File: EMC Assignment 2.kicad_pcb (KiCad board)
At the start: 4 copper layers, 120 x 53 mm, 91 parts, among them IC1 LP2985AIM5-3.0_NOPB, J1 M40-3200445R, U1 LT8636, U2 ATMEGA16U2-MU, U3 ATMEGA328P-PU, U8 OPA4350EA_250, X2 USB, Y1 16MHz, Y2 16M

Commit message: Good state
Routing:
- net /PB4: track 35.9 -> 28.1 mm

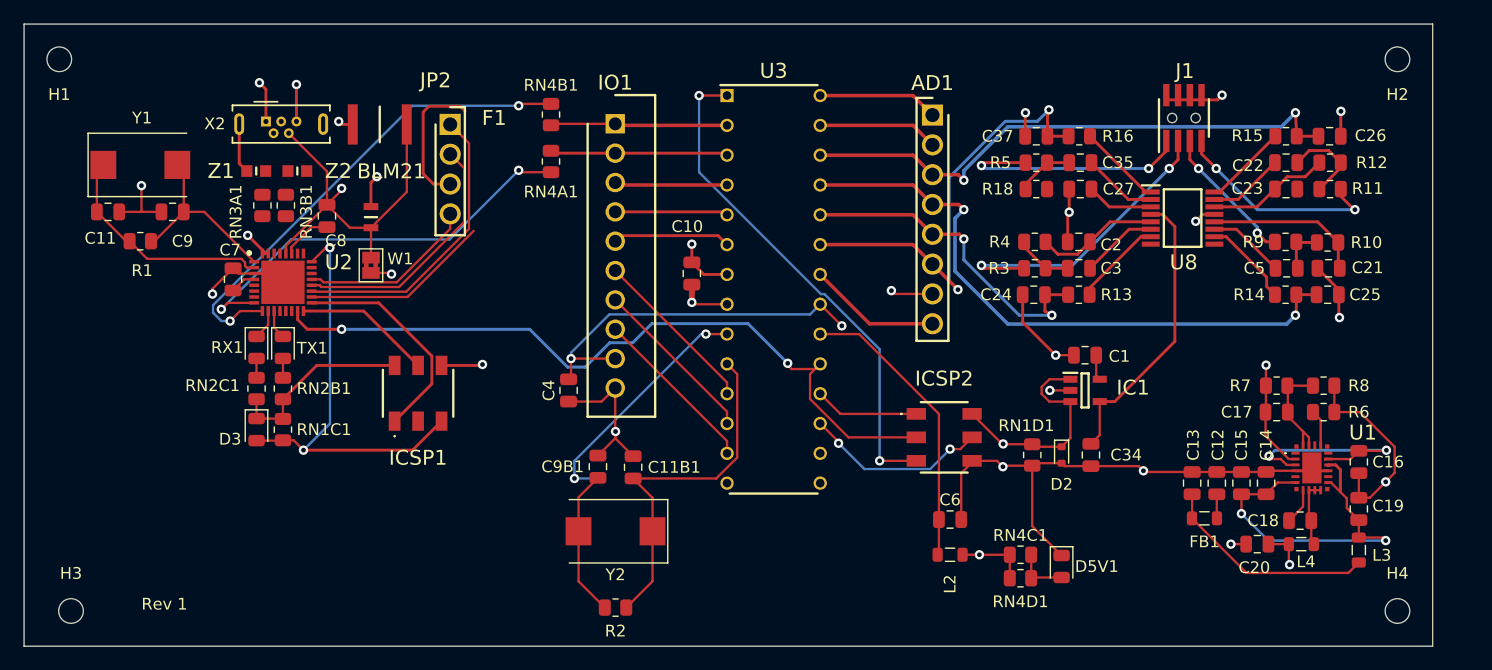
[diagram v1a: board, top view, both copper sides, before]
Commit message: Fixed majority of DRC issues. Only differential pair needs to be fixed up
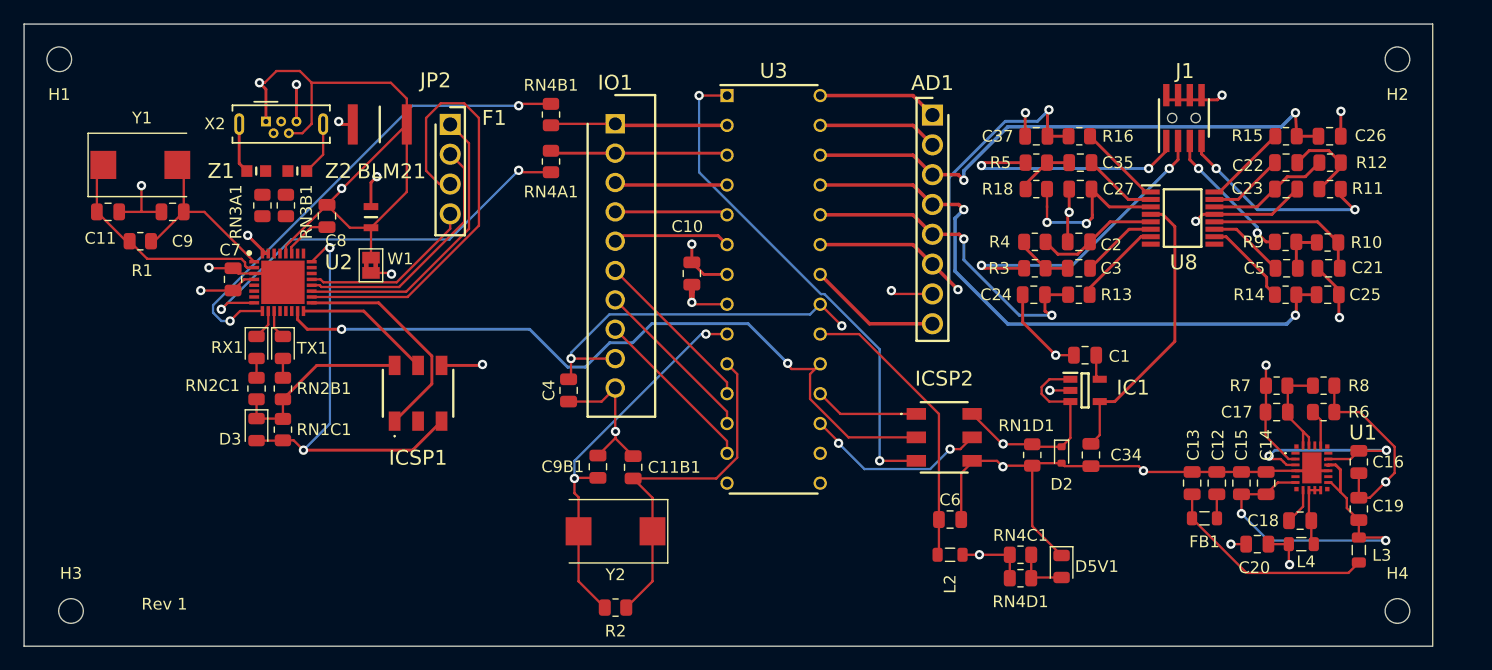
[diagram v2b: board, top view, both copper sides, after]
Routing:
- net /UGND: track 35.7 -> 57.9 mm
- net /PB4: track 28.1 -> 38.5 mm
- net Net-(U8-+IN_A): track 5.68 -> 15.4 mm, vias 0 -> 2
- net GND: track 139.9 -> 147.0 mm
- net Net-(X2-Shield): track 4.27 -> 8.85 mm
- net +5V: track 49.3 -> 52.0 mm, vias 7 -> 8
- net Net-(U3-PB6_(PCINT6/XTAL1/TOSC1)): track 33.6 -> 33.1 mm

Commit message: Fixed differential lines with new USB footprint and 3D model. No DRC errors
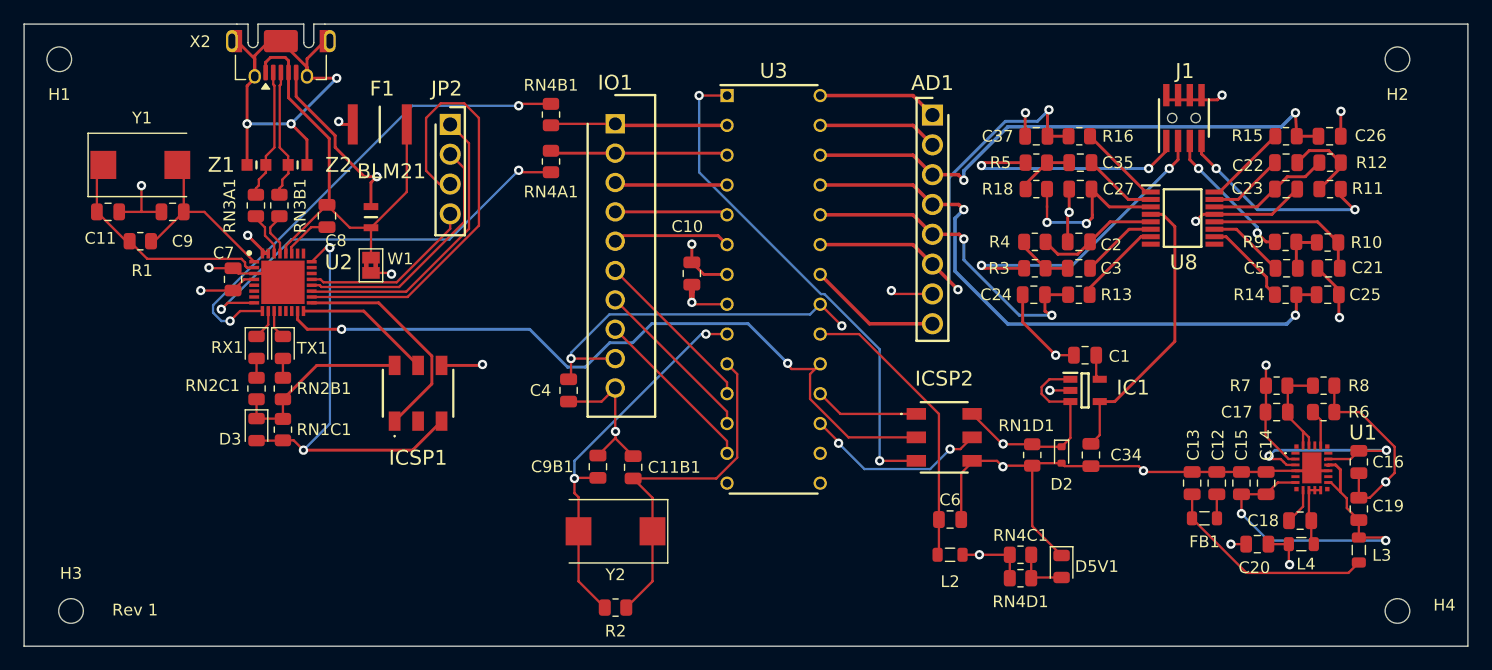
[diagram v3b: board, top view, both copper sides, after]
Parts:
- X2: footprint Connector_USB:USB_Micro-B_Wuerth_614105150721_Vertical -> Connector_USB:USB_Micro-AB_Molex_47590-0001
- moved X2 7.31 mm to (33.9, 13.1), turned to 180 degrees
- moved RN3A1 0.55 mm to (31.8, 27.5)
- moved RN3B1 0.55 mm to (33.8, 27.5)
- moved Z1 0.52 mm to (31.8, 24.0)
- moved Z2 0.52 mm to (35.3, 24.0)
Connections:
- net /D+ renamed /USBD+
- net /D- renamed /USBD-
- net Net-(U2-D+) renamed /Pad-D+
- net Net-(U2-D-) renamed /Pad-D-
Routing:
- net Net-(X2-Shield): track 8.85 -> 39.2 mm, vias 0 -> 3
- net /UGND: track 57.9 -> 39.7 mm, vias 2 -> 0
- net /USBD+: track 0.00 -> 11.1 mm
- net /USBD-: track 0.33 -> 11.1 mm
- net GND: track 147.0 -> 156.2 mm, vias 21 -> 20
- net /Pad-D+: track 0.00 -> 3.85 mm
- net /Pad-D-: track 0.00 -> 3.83 mm
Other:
- board size 120 x 53 mm -> 123 x 53 mm
